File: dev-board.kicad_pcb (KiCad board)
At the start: 2 copper layers, 29 x 51.9 mm, 21 parts, among them J1 TYPE-C-31-M-12, J2 Conn_01x20_Pin, J3 Conn_01x20_Pin, SW1 TS-1088-AR02016, SW2 TS-1088-AR02016, U2 ESP32-S3-WROOM-1, U3 LD1117S33TR_SOT223

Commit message: Minor Changes
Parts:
- removed C1, C4: 10u, Capacitor_SMD:C_0603_1608Metric
- removed C2: 22u, Capacitor_SMD:C_0603_1608Metric
- removed C3: 100n, Capacitor_SMD:C_0603_1608Metric
- removed D1: RED, LED_SMD:LED_0603_1608Metric
- removed D2: GREEN, LED_SMD:LED_0603_1608Metric
- removed D3: BLUE, LED_SMD:LED_0603_1608Metric
- removed J1: TYPE-C-31-M-12, TYPE-C-31-M-12:HRO_TYPE-C-31-M-12
- removed J2, J3: Conn_01x20_Pin, Connector_PinHeader_2.54mm:PinHeader_1x20_P2.54mm_Vertical
- removed R1, R2, R4, R5, R6: 5.1K, Resistor_SMD:R_0603_1608Metric
- removed SW1, SW2: TS-1088-AR02016, easyeda2kicad:SW-SMD_L3.9-W3.0-P4.45
- added C11: 100nF, Capacitor_SMD:C_1206_3216Metric_Pad1.33x1.80mm_HandSolder, F.Cu at (94.4, 38.5)
- added C12: 1uF, Capacitor_SMD:C_1206_3216Metric_Pad1.33x1.80mm_HandSolder, F.Cu at (94.4, 41.9)
- added C13: 22uF, Capacitor_SMD:C_1206_3216Metric_Pad1.33x1.80mm_HandSolder, F.Cu at (94.4, 45.2)
- added C14: 10uF, Capacitor_SMD:C_1206_3216Metric_Pad1.33x1.80mm_HandSolder, F.Cu at (94.4, 48.6)
- added C15: 1uF, Capacitor_SMD:C_1206_3216Metric_Pad1.33x1.80mm_HandSolder, F.Cu at (94.4, 52.0)
- added C16: 1uF, Capacitor_SMD:C_1206_3216Metric_Pad1.33x1.80mm_HandSolder, F.Cu at (94.4, 55.3)
- added D4: GREEN 20mA@2V, LED_SMD:LED_1206_3216Metric_Pad1.42x1.75mm_HandSolder, F.Cu at (108.0, 53.8)
- added D5: GREEN 20mA@2V, LED_SMD:LED_1206_3216Metric_Pad1.42x1.75mm_HandSolder, F.Cu at (108.0, 57.2)
- added L1: 33uH, VLS6045EX_330M:IND_VLS6045EX-330M, F.Cu at (101.2, 55.9)
- added R12: 1.1k, Resistor_SMD:R_1206_3216Metric_Pad1.30x1.75mm_HandSolder, F.Cu at (109.8, 46.6)
- added R13: 120R, Resistor_SMD:R_1206_3216Metric_Pad1.30x1.75mm_HandSolder, F.Cu at (109.8, 49.9)
- added U2: L6981N50DR, L6981N50DR:SO8L_L6981N33DR_STM-M, F.Cu at (102.1, 48.5)
- C5: value 10u -> 1u
- U3: value LD1117S33TR_SOT223 -> TLV1117LV33DCYR; footprint Package_TO_SOT_SMD:SOT-223-3_TabPin2 -> TLV1117LV33DCYR:VREG_TLV1117LV33DCYR
- moved U3 43.7 mm to (102.7, 40.9), turned to 0 degrees
- moved C5 30.4 mm to (116.8, 38.1), turned to 0 degrees
- moved R3 29.6 mm to (116.8, 40.6), turned to 0 degrees
- moved U1 10.2 mm to (135.2, 57.4)
- renumbered U2 to U1
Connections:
- C5 pad 1: EN -> unconnected-(C5-Pad1)
- C5 pad 2: GND -> unconnected-(C5-Pad2)
- R3 pad 1: +3V3 -> +3.3V
- U3 pad 2: +3V3 -> unconnected-(U3-OUT_2-Pad2)
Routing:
- net GND: track 114.6 -> 21.1 mm, vias 38 -> 12
- net +5V: track 70.1 -> 0.00 mm, vias 3 -> 0
- net +3V3: track 61.6 -> 0.00 mm, vias 2 -> 0
- net EN: track 59.4 -> 0.00 mm, vias 3 -> 0
- net D-: track 56.2 -> 0.00 mm, vias 2 -> 0
- net D+: track 56.1 -> 0.00 mm, vias 3 -> 0
- net GPIO12: track 36.1 -> 0.00 mm
- net GPIO13: track 35.7 -> 0.00 mm, vias 1 -> 0
- net GPIO0: track 35.3 -> 0.00 mm, vias 1 -> 0
- net GPIO11: track 32.6 -> 0.00 mm
- net GPIO14: track 32.6 -> 0.00 mm, vias 1 -> 0
- net GPIO21: track 30.5 -> 0.00 mm, vias 1 -> 0
- net GPIO10: track 29.6 -> 0.00 mm
- net GPIO9: track 26.5 -> 0.00 mm
- net GPIO47: track 26.5 -> 0.00 mm, vias 1 -> 0
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- removed copper zone on B.Cu, net GND
- removed copper zone on F.Cu, net GND
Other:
- board outline removed
- board text removed: "0"
- board text removed: "1"
- board text removed: "10"
- board text removed: "11"
- board text removed: "12"
- board text removed: "13"
- board text removed: "14"
- board text removed: "15"
- board text removed: "16"
- board text removed: "17"
- board text removed: "18"
- board text removed: "19"
- board text removed: "2"
- board text removed: "20"
- board text removed: "21"
- board text removed: "3"
- board text removed: "35"
- board text removed: "36"
- board text removed: "37"
- board text removed: "38"
- board text removed: "39"
- board text removed: "3V3"
- board text removed: "4"
- board text removed: "40"
- board text removed: "41"
- board text removed: "42"
- board text removed: "43"
- board text removed: "44"
- board text removed: "45"
- board text removed: "46"
- board text removed: "47"
- board text removed: "48"
- board text removed: "5"
- board text removed: "5V"
- board text removed: "6"
- board text removed: "7"
- board text removed: "8"
- board text removed: "9"
- board text removed: "BOOT"
- board text removed: "EN"
- board text removed: "GND"
- board text removed: "RESET"
- board text removed: "WayWayWay"

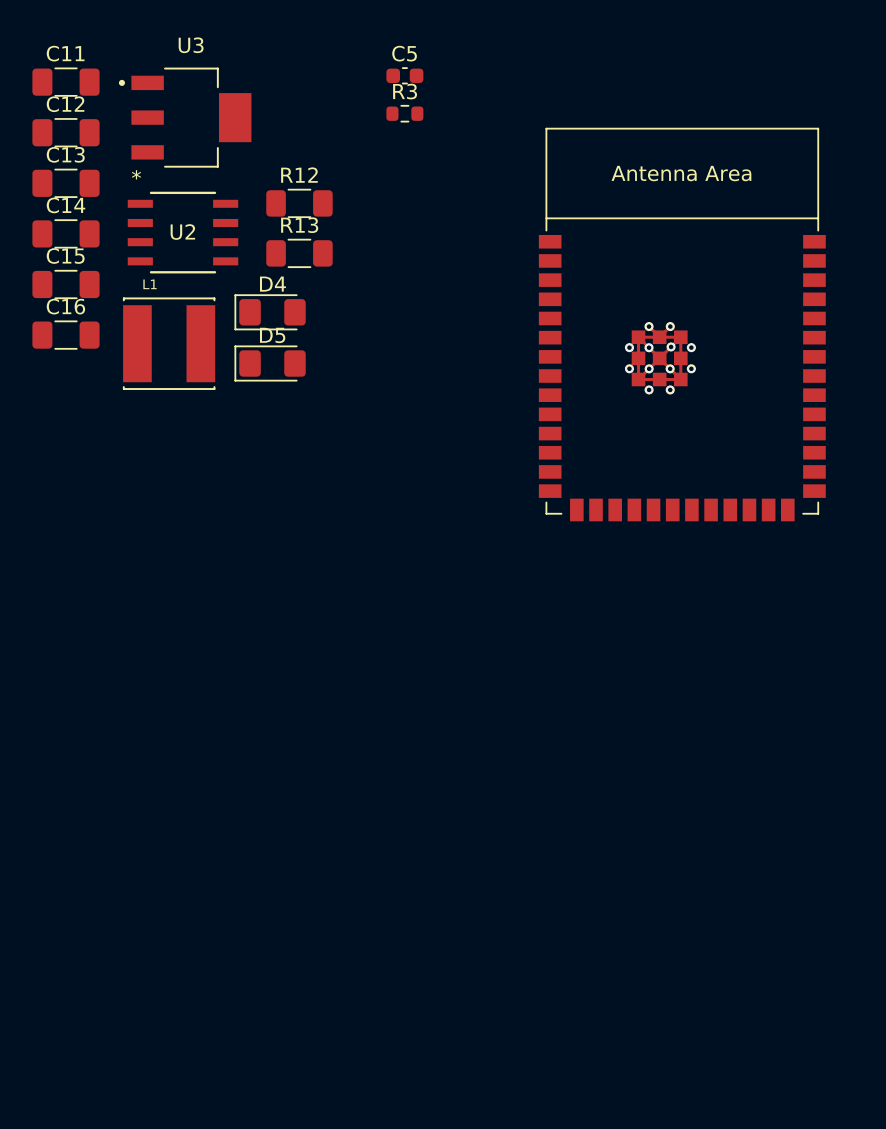
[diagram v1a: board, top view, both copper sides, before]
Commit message: Copy and Adjust Parts from previous version
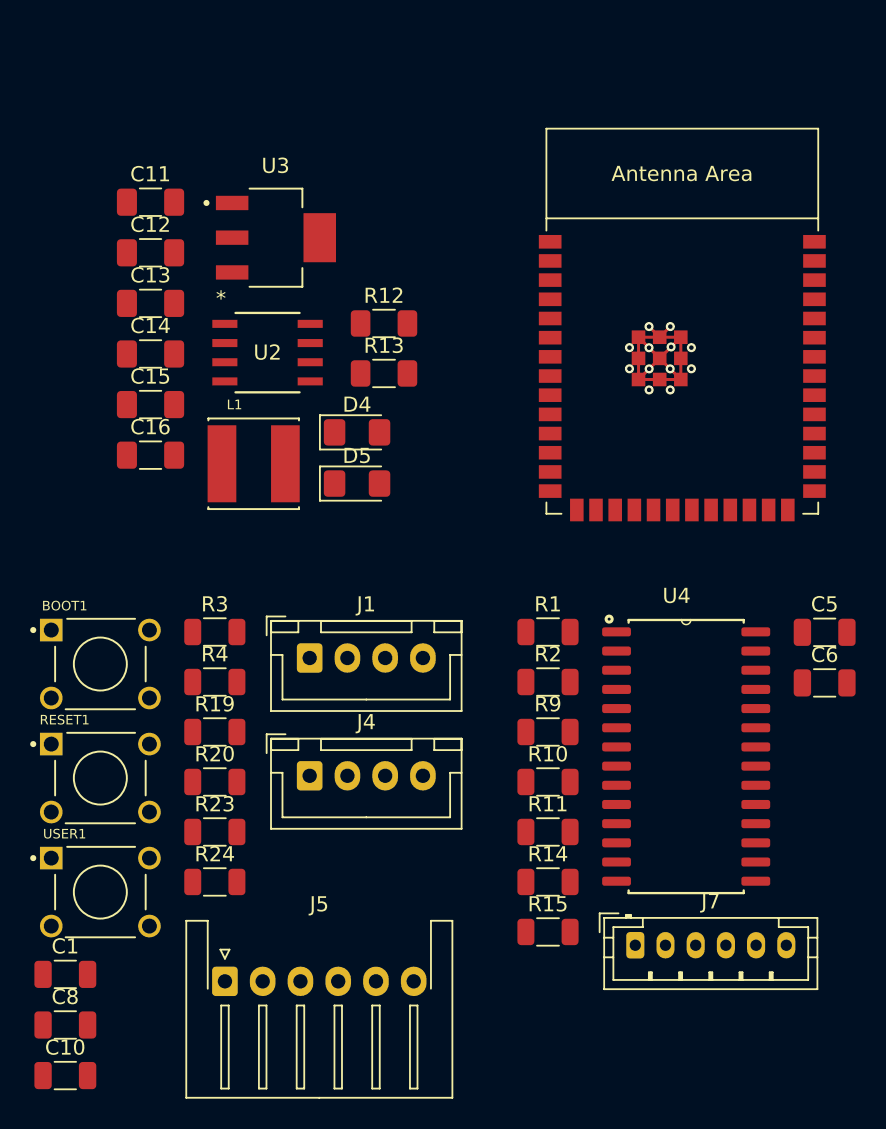
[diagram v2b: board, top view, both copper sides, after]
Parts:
- added BOOT1: 1825910-6, Switch 1825910_6:SW_1825910-6-4, F.Cu at (96.7, 77.1)
- added C1: 100nF, Capacitor_SMD:C_1206_3216Metric, F.Cu at (94.3, 97.6)
- added C10: 100nF, Capacitor_SMD:C_1206_3216Metric, F.Cu at (94.3, 104.3)
- added C6: 100nF, Capacitor_SMD:C_1206_3216Metric, F.Cu at (144.6, 78.3)
- added C8: 100nF, Capacitor_SMD:C_1206_3216Metric, F.Cu at (94.3, 101.0)
- added J1: UART_0, Connector_JST:JST_XH_B4B-XH-A_1x04_P2.50mm_Vertical, F.Cu at (110.5, 76.7)
- added J4: UART_1, Connector_JST:JST_XH_B4B-XH-A_1x04_P2.50mm_Vertical, F.Cu at (110.5, 84.5)
- added J5: UART_2, Connector_JST:JST_XH_S6B-XH-A-1_1x06_P2.50mm_Horizontal, F.Cu at (104.9, 98.1)
- added J7: Button Header, Connector_JST:JST_PH_B6B-PH-K_1x06_P2.00mm_Vertical, F.Cu at (132.1, 95.7)
- added R1: 0, Resistor_SMD:R_1206_3216Metric, F.Cu at (126.3, 75.0)
- added R10: 10k, Resistor_SMD:R_1206_3216Metric, F.Cu at (126.3, 84.9)
- added R11: 10k, Resistor_SMD:R_1206_3216Metric, F.Cu at (126.3, 88.2)
- added R14: 0, Resistor_SMD:R_1206_3216Metric, F.Cu at (126.3, 91.5)
- added R15: 0, Resistor_SMD:R_1206_3216Metric, F.Cu at (126.3, 94.8)
- added R19: 100, Resistor_SMD:R_1206_3216Metric, F.Cu at (104.2, 81.6)
- added R2: 10k, Resistor_SMD:R_1206_3216Metric, F.Cu at (126.3, 78.3)
- added R20: 4.7k, Resistor_SMD:R_1206_3216Metric, F.Cu at (104.2, 84.9)
- added R23: 100, Resistor_SMD:R_1206_3216Metric, F.Cu at (104.2, 88.2)
- added R24: 4.7k, Resistor_SMD:R_1206_3216Metric, F.Cu at (104.2, 91.5)
- added R4: 4.7k, Resistor_SMD:R_1206_3216Metric, F.Cu at (104.2, 78.3)
- added R9: 10k, Resistor_SMD:R_1206_3216Metric, F.Cu at (126.3, 81.6)
- added RESET1: 1825910-6, Switch 1825910_6:SW_1825910-6-4, F.Cu at (96.7, 84.6)
- added U4: MCP23017T-E_SO, MCP23017T_E_SO:SOIC127P1030X265-28N, F.Cu at (135.4, 83.2)
- added USER1: 1825910-6, Switch 1825910_6:SW_1825910-6-4, F.Cu at (96.7, 92.2)
- C5: value 1u -> 100nF; footprint Capacitor_SMD:C_0603_1608Metric -> Capacitor_SMD:C_1206_3216Metric
- R3: value 5.1K -> 100; footprint Resistor_SMD:R_0603_1608Metric -> Resistor_SMD:R_1206_3216Metric
- moved C5 46.2 mm to (144.6, 75.0)
- moved R3 36.6 mm to (104.2, 75.0)
- moved R12 9.72 mm to (115.4, 54.5)
- moved R13 9.72 mm to (115.4, 57.8)
- moved U2 9.72 mm to (107.7, 56.5)
- moved C11 9.72 mm to (100.0, 46.5)
- moved C12 9.72 mm to (100.0, 49.9)
- moved C13 9.72 mm to (100.0, 53.2)
- moved C16 9.72 mm to (100.0, 63.2)
- moved D4 9.72 mm to (113.6, 61.7)
- moved L1 9.72 mm to (106.8, 63.8)
- moved U3 9.72 mm to (108.3, 48.9)
- moved C14 9.72 mm to (100.0, 56.5)
- moved C15 9.72 mm to (100.0, 59.9)
- moved D5 9.72 mm to (113.6, 65.1)
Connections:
- C5 pad 1: unconnected-(C5-Pad1) -> +3.3V
- C5 pad 2: unconnected-(C5-Pad2) -> GND
- R3 pad 1: +3.3V -> GND Panel
- R3 pad 2: EN -> Net-(C1-Pad1)
- U1 pad 10: GPIO17 -> UART2_TX
- U1 pad 11: GPIO18 -> UART2_RX
- U1 pad 36: GPIO44 -> UART0_RX
- U1 pad 37: GPIO43 -> UART0_TX
- U1 pad 4: GPIO4 -> UART1_TX
- U1 pad 5: GPIO5 -> UART1_RX
- U1 pad 6: GPIO6 -> Interrupt_B
- U1 pad 7: GPIO7 -> Interrupt_A
